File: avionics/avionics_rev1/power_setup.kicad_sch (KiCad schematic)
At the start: 62 parts, among them J1 Conn_01x02, J2 Conn_01x02, J4 USB_C_Receptacle_USB2.0_16P, Q1 DMN2056U-7, U1 LMR604063SBRAKRQ1, U13 TPS2121RUXR, U5 TPS2121RUXR, U6 TLV7041DBVR, U7 TMUX1511RSVR

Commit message: cleaned up schematics after codex work
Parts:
- removed R5: 120 1%, Resistor_SMD:R_0201_0603Metric, symbol Device:R_Small_US
- added C45, C53, C54, C55: 10n 16V, Capacitor_SMD:C_0402_1005Metric, symbol rocketry_library:GRM155R71C103KA01D
- added R5: 120 1%, Resistor_SMD:R_0402_1005Metri, symbol rocketry_library:RC0402FR-071KL
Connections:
- net +3.3V: now also R5.2
- net ADC_MAIN: now also C54.1
- net ADC_USB: now also C53.1
- net GND: now also C45.2, C53.2, C54.2, C55.2; no longer U7.13 (D4), U7.14 (S4), U7.15 (SEL4)
- net SENSE_EN: now also U7.15 (SEL4)
- net at D1.2 (A): now also R5.1
- net ADC_TPS_OUT renamed ADC_PYRO_POWER
- net ADC_PYRO_POWER: now also C55.1
- net SENS_BATT renamed SENS_LOGIC_VIN
- net SENS_LOGIC_VIN: now also U7.14 (S4)
- new net ADC_LOGIC: C45.1, U7.13 (D4)
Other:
- note added: "D1: existing LED reused for MCU status. PB6 high = ON; 1k limits current to ~1.2 mA."
- note added: "U7 CH4: VIN_LOGIC divider -> ADC_LOGIC / PB1. SENSE_EN low at reset; wait >=5 ms after enable before ADC sampling."
- note added: "VIN_LOGIC sense; not raw battery R3/R4: 220k/47k (ratio 0.1760) 16.8 V -> 2.957 V at SENS_LOGIC_VIN"
- note removed: "R = (V_sup - V_forward) / I_forward R = (3.3 - 2.1) / 0.010A = 120 ohm"
- note removed: "VIN_LOGIC sense; not raw battery R3/R4: 220k/47k (ratio 0.1760) 16.8 V -> 2.957 V at SENS_BATT"
- moved on the sheet: C36, R44, U7

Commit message: saving MCU work before using codex
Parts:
- added TP3, TP4, TP5, TP6, TP7, TP8, TP9: TestPoint, symbol Connector:TestPoint
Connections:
- net +3.3V: now also TP3.1
- net PYRO_POWER: now also TP8.1
- net PYRO_POWER_SENS: now also TP9.1
- net VIN_LOGIC: now also TP4.1
- net VIN_MAIN_BATT: now also TP6.1
- net VIN_PYRO_BATT: now also TP5.1
- net at R25.2, R26.1, U5.5 (OV1)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: now also TP7.1

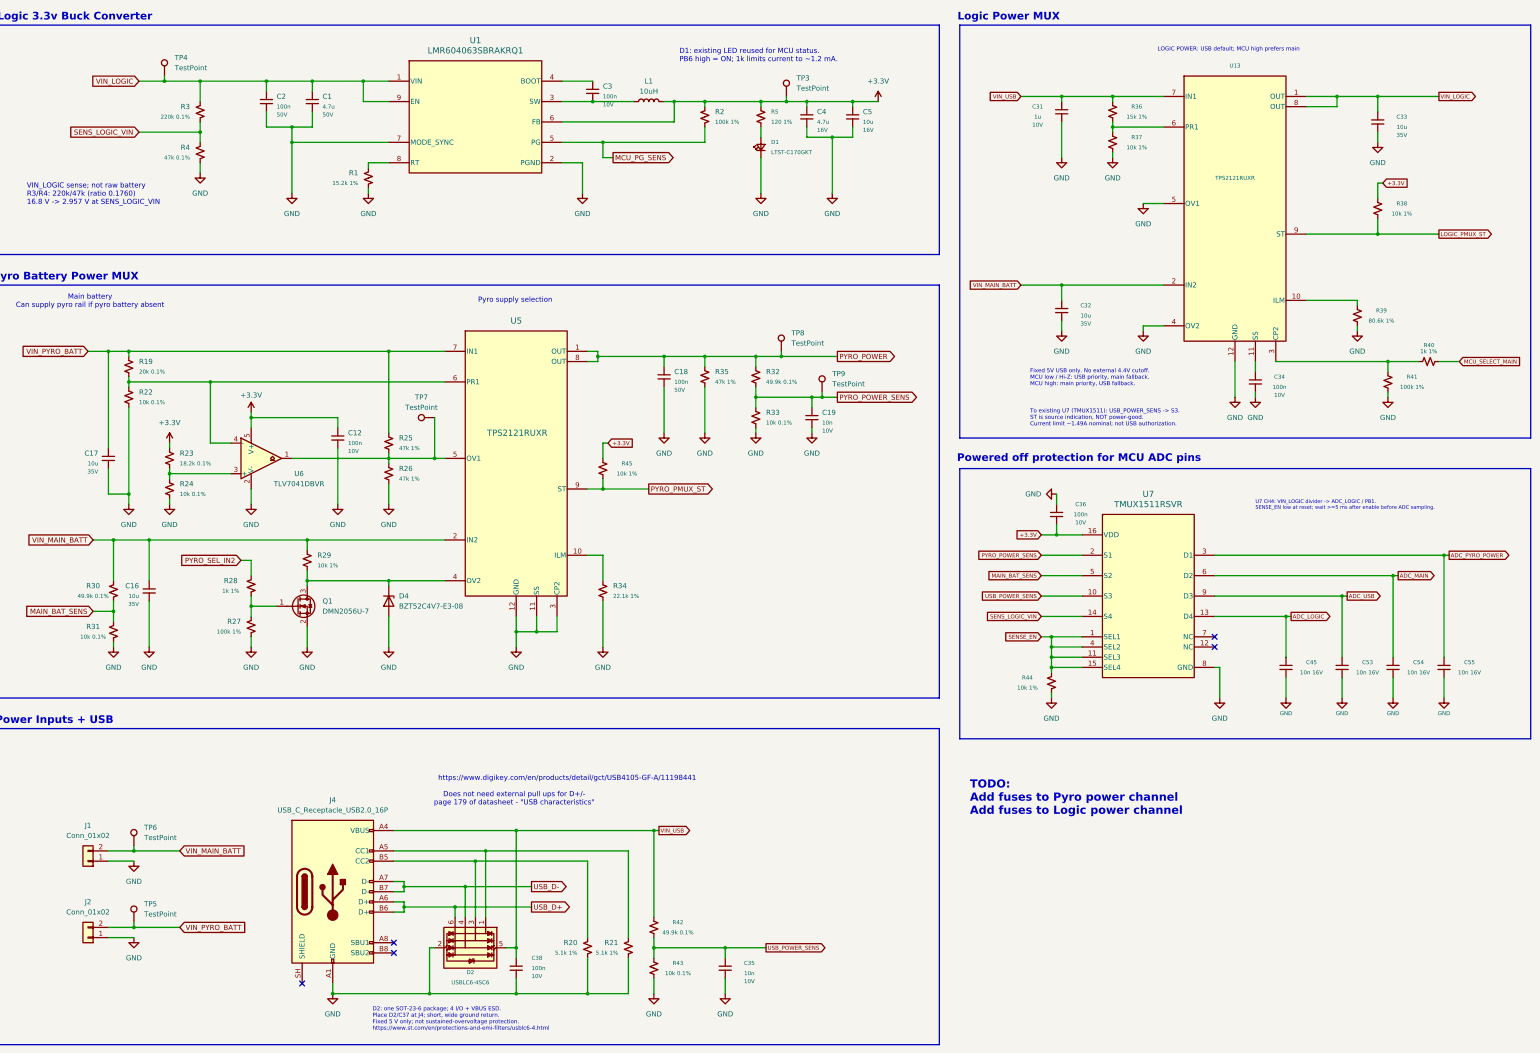
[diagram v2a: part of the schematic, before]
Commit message: fixed ERC errors
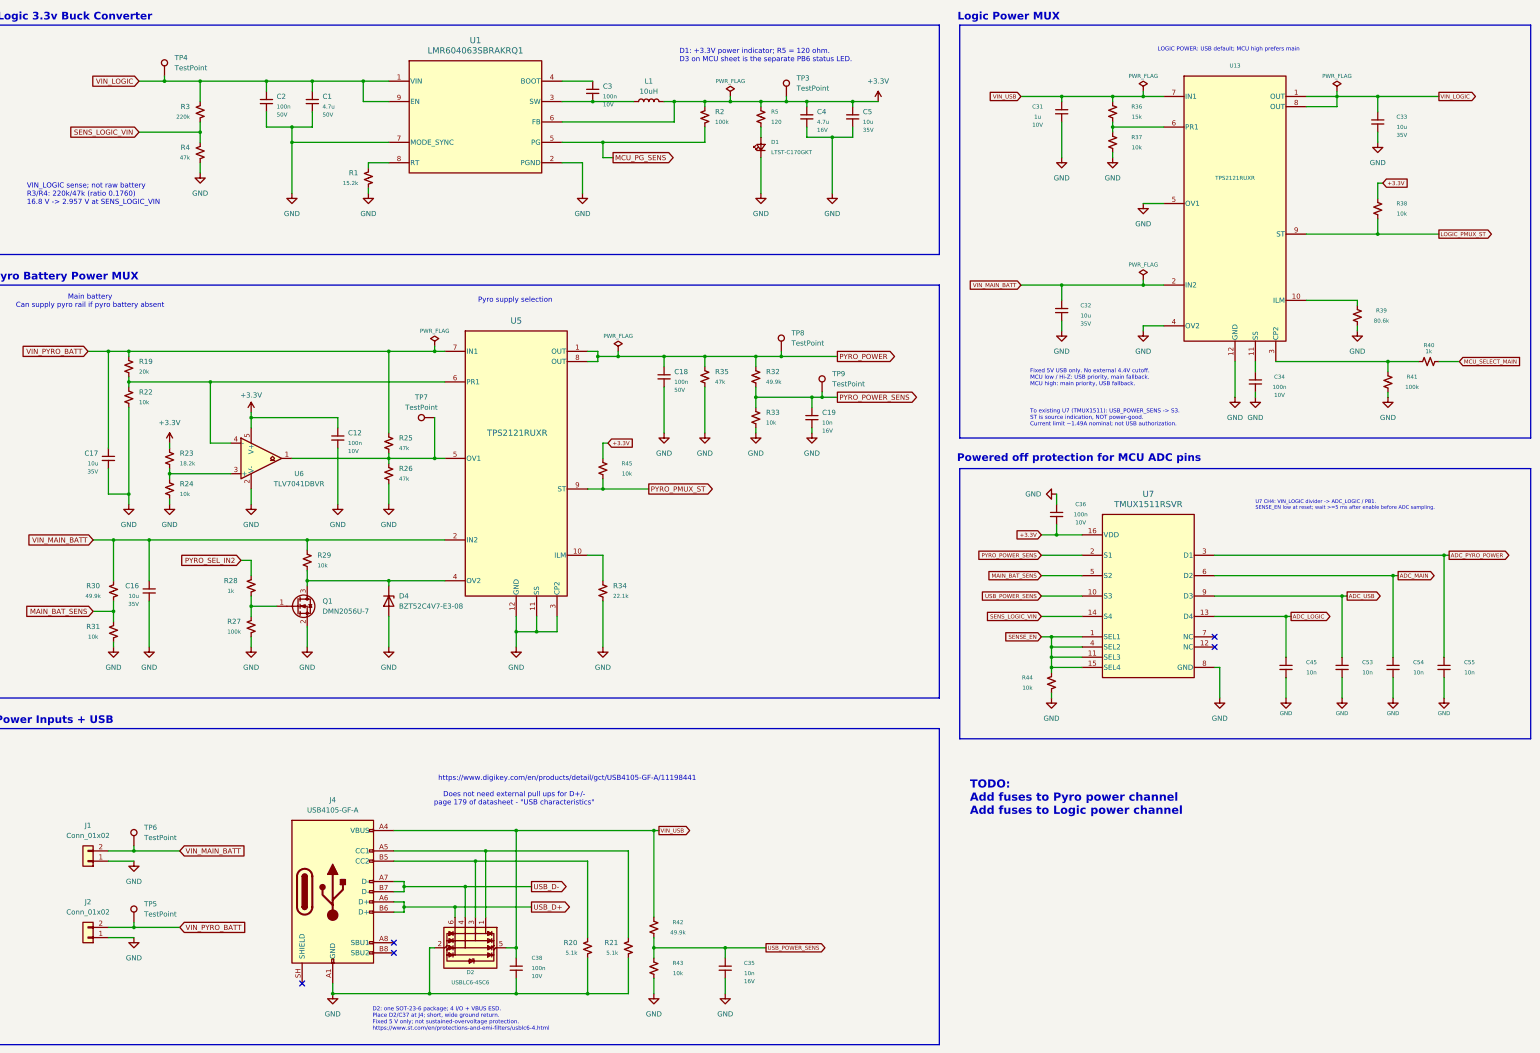
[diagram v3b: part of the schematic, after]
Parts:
- C1: symbol Device:C_Small -> rocketry_library:C2012X5R1H475K125AB; Dielectric X7R -> X5R; DigiKey (none) -> https://www.digikey.com/en/products/detail/tdk/C2012X5R1H47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; MPN (none) -> C2012X5R1H475K125AB; Manufacturer (none) -> TDK; Tolerance (none) -> 10%
- C12, C34, C36, C38: symbol Device:C_Small -> rocketry_library:GRM155R71A104KA01D; DigiKey (none) -> https://www.digikey.com/en/products/detail/murata-electroni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; MPN (none) -> GRM155R71A104KA01D; Tolerance (none) -> 10%
- C16, C17, C32, C33: symbol Device:C_Small -> rocketry_library:GRM21BR6YA106KE43L; Dielectric X7R -> X5R; DigiKey (none) -> https://www.digikey.com/en/products/detail/murata-electroni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; MPN (none) -> GRM21BR6YA106KE43L; Manufacturer (none) -> Murata; Tolerance (none) -> 10%
- C18, C2: symbol Device:C_Small -> rocketry_library:GRM155R71H104KE14D; DigiKey (none) -> https://www.digikey.com/en/products/detail/murata-electroni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; MPN (none) -> GRM155R71H104KE14D; Manufacturer (none) -> Murata; Tolerance (none) -> 10%
- C19, C35: symbol Device:C_Small -> rocketry_library:GRM155R71C103KA01D; DigiKey (none) -> https://www.digikey.com/en/products/detail/murata-electroni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; MPN (none) -> GRM155R71C103KA01D; Tolerance (none) -> 10%; Voltage 10V -> 16V
- C3: footprint Capacitor_SMD:C_0201_0603Metric -> Capacitor_SMD:C_0402_1005Metric; symbol Device:C_Small -> rocketry_library:GRM155R71A104KA01D; DigiKey (none) -> https://www.digikey.com/en/products/detail/murata-electroni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; MPN (none) -> GRM155R71A104KA01D; Tolerance (none) -> 10%
- C31: footprint Capacitor_SMD:C_0402_1005Metric -> Capacitor_SMD:C_0603_1608Metric; symbol Device:C_Small -> rocketry_library:C1608X7R1A105K080AC; DigiKey (none) -> https://www.digikey.com/en/products/detail/tdk/C1608X7R1A10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; MPN (none) -> C1608X7R1A105K080AC; Tolerance (none) -> 10%
- C4: symbol Device:C_Small -> rocketry_library:GRM188R61C475KE11D; Dielectric X7R -> X5R; DigiKey (none) -> https://www.digikey.com/en/products/detail/murata-electroni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; MPN (none) -> GRM188R61C475KE11D; Manufacturer (none) -> Murata; Tolerance (none) -> 10%
- C45, C53, C54, C55: value 10n 16V -> 10n
- C5: symbol Device:C_Small -> rocketry_library:GRM21BR6YA106KE43L; Dielectric X7R -> X5R; DigiKey (none) -> https://www.digikey.com/en/products/detail/murata-electroni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; MPN (none) -> GRM21BR6YA106KE43L; Manufacturer (none) -> Murata; Tolerance (none) -> 10%; Voltage 16V -> 35V
- J4: value USB_C_Receptacle_USB2.0_16P -> USB4105-GF-A; footprint (none) -> Connector_USB:USB_C_Receptacle_GCT_USB4105-xx-A_16P_TopMnt_Horizontal; symbol Connector:USB_C_Receptacle_USB2.0_16P -> rocketry_library:USB4105-GF-A; DigiKey (none) -> https://www.digikey.com/en/products/detail/gct/USB4105-GF-A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; MPN (none) -> USB4105-GF-A; Manufacturer (none) -> GCT
- R1: value 15.2k 1% -> 15.2k; footprint Resistor_SMD:R_0201_0603Metric -> Resistor_SMD:R_0402_1005Metric; symbol Device:R_Small_US -> rocketry_library:RN73R1ETTP1522B25; DigiKey (none) -> https://www.digikey.com/en/products/detail/koa-speer-electr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; MPN (none) -> RN73R1ETTP1522B25; Manufacturer (none) -> KOA Speer; Power (none) -> 0.0625W; Tolerance 1% -> 0.1%; Voltage (none) -> 50V
- R19: value 20k 0.1% -> 20k; footprint (none) -> Resistor_SMD:R_0402_1005Metric; symbol Device:R_Small_US -> rocketry_library:RT0402BRD0720KL; DigiKey (none) -> https://www.digikey.com/en/products/detail/yageo/RT0402BRD0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; MPN (none) -> RT0402BRD0720KL; Manufacturer (none) -> Yageo; Power (none) -> 0.0625W; Voltage (none) -> 50V
- R2, R41: value 100k 1% -> 100k; footprint Resistor_SMD:R_0201_0603Metric -> Resistor_SMD:R_0402_1005Metric; symbol Device:R_Small_US -> rocketry_library:RC0402FR-07100KL; DigiKey (none) -> https://www.digikey.com/en/products/detail/yageo/RC0402FR-0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; MPN (none) -> RC0402FR-07100KL; Power (none) -> 0.063W; Voltage (none) -> 50V
- R20, R21: value 5.1k 1% -> 5.1k; footprint Resistor_SMD:R_0201_0603Metric -> Resistor_SMD:R_0402_1005Metric; symbol Device:R_Small_US -> rocketry_library:RC0402FR-075K1L; DigiKey (none) -> https://www.digikey.com/en/products/detail/yageo/RC0402FR-0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; MPN (none) -> RC0402FR-075K1L; Manufacturer (none) -> Yageo; Power (none) -> 0.0625W; Voltage (none) -> 50V
- R22, R24, R31, R33: value 10k 0.1% -> 10k; footprint (none) -> Resistor_SMD:R_0402_1005Metric; symbol Device:R_Small_US -> rocketry_library:RT0402BRD0710KL; DigiKey (none) -> https://www.digikey.com/en/products/detail/yageo/RT0402BRD0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; MPN (none) -> RT0402BRD0710KL; Manufacturer (none) -> Yageo; Power (none) -> 0.0625W; Voltage (none) -> 50V
- R23: value 18.2k 0.1% -> 18.2k; footprint (none) -> Resistor_SMD:R_0402_1005Metric; symbol Device:R_Small_US -> rocketry_library:RT0402BRD0718K2L; DigiKey (none) -> https://www.digikey.com/en/products/detail/yageo/RT0402BRD0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; MPN (none) -> RT0402BRD0718K2L; Manufacturer (none) -> Yageo; Power (none) -> 0.0625W; Voltage (none) -> 50V
- R25, R26, R35: value 47k 1% -> 47k; footprint (none) -> Resistor_SMD:R_0402_1005Metric; symbol Device:R_Small_US -> rocketry_library:RC0402FR-0747KL; DigiKey (none) -> https://www.digikey.com/en/products/detail/yageo/RC0402FR-0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; MPN (none) -> RC0402FR-0747KL; Manufacturer (none) -> Yageo; Power (none) -> 0.0625W; Voltage (none) -> 50V
- R27: value 100k 1% -> 100k; footprint (none) -> Resistor_SMD:R_0402_1005Metric; symbol Device:R_Small_US -> rocketry_library:RC0402FR-07100KL; DigiKey (none) -> https://www.digikey.com/en/products/detail/yageo/RC0402FR-0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; MPN (none) -> RC0402FR-07100KL; Power (none) -> 0.063W; Voltage (none) -> 50V
- R28: value 1k 1% -> 1k; footprint (none) -> Resistor_SMD:R_0402_1005Metric; symbol Device:R_Small_US -> rocketry_library:RC0402FR-071KL; DigiKey (none) -> https://www.digikey.com/en/products/detail/yageo/RC0402FR-0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; MPN (none) -> RC0402FR-071KL; Power (none) -> 0.063W; Voltage (none) -> 50V
- R29: value 10k 1% -> 10k; footprint (none) -> Resistor_SMD:R_0402_1005Metric; symbol Device:R_Small_US -> rocketry_library:RC0402FR-0710KL; DigiKey (none) -> https://www.digikey.com/en/products/detail/yageo/RC0402FR-0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; MPN (none) -> RC0402FR-0710KL; Voltage (none) -> 50V
- R3: value 220k 0.1% -> 220k; footprint Resistor_SMD:R_0201_0603Metric -> Resistor_SMD:R_0402_1005Metric; symbol Device:R_Small_US -> rocketry_library:RT0402BRD07220KL; DigiKey (none) -> https://www.digikey.com/en/products/detail/yageo/RT0402BRD0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; MPN (none) -> RT0402BRD07220KL; Manufacturer (none) -> Yageo; Power (none) -> 0.0625W; Voltage (none) -> 50V
- R30, R32: value 49.9k 0.1% -> 49.9k; footprint (none) -> Resistor_SMD:R_0402_1005Metric; symbol Device:R_Small_US -> rocketry_library:RT0402BRD0749K9L; DigiKey (none) -> https://www.digikey.com/en/products/detail/yageo/RT0402BRD0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; MPN (none) -> RT0402BRD0749K9L; Manufacturer (none) -> Yageo; Power (none) -> 0.0625W; Voltage (none) -> 50V
- R34: value 22.1k 1% -> 22.1k; footprint (none) -> Resistor_SMD:R_0402_1005Metric; symbol Device:R_Small_US -> rocketry_library:RC0402FR-0722K1L; DigiKey (none) -> https://www.digikey.com/en/products/detail/yageo/RC0402FR-0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; MPN (none) -> RC0402FR-0722K1L; Manufacturer (none) -> Yageo; Power (none) -> 0.0625W; Voltage (none) -> 50V
- R36: value 15k 1% -> 15k; footprint Resistor_SMD:R_0201_0603Metric -> Resistor_SMD:R_0402_1005Metric; symbol Device:R_Small_US -> rocketry_library:RC0402FR-0715KL; DigiKey (none) -> https://www.digikey.com/en/products/detail/yageo/RC0402FR-0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; MPN (none) -> RC0402FR-0715KL; Manufacturer (none) -> Yageo; Power (none) -> 0.0625W; Voltage (none) -> 50V
- R37, R38, R44, R45: value 10k 1% -> 10k; footprint Resistor_SMD:R_0201_0603Metric -> Resistor_SMD:R_0402_1005Metric; symbol Device:R_Small_US -> rocketry_library:RC0402FR-0710KL; DigiKey (none) -> https://www.digikey.com/en/products/detail/yageo/RC0402FR-0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; MPN (none) -> RC0402FR-0710KL; Voltage (none) -> 50V
- R39: value 80.6k 1% -> 80.6k; footprint Resistor_SMD:R_0201_0603Metric -> Resistor_SMD:R_0402_1005Metric; symbol Device:R_Small_US -> rocketry_library:RC0402FR-0780K6L; DigiKey (none) -> https://www.digikey.com/en/products/detail/yageo/RC0402FR-0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; MPN (none) -> RC0402FR-0780K6L; Manufacturer (none) -> Yageo; Power (none) -> 0.0625W; Voltage (none) -> 50V
- R4: value 47k 0.1% -> 47k; footprint Resistor_SMD:R_0201_0603Metric -> Resistor_SMD:R_0402_1005Metric; symbol Device:R_Small_US -> rocketry_library:RT0402BRD0747KL; DigiKey (none) -> https://www.digikey.com/en/products/detail/yageo/RT0402BRD0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; MPN (none) -> RT0402BRD0747KL; Manufacturer (none) -> Yageo; Power (none) -> 0.0625W; Voltage (none) -> 50V
- R40: value 1k 1% -> 1k; footprint Resistor_SMD:R_0201_0603Metric -> Resistor_SMD:R_0402_1005Metric; symbol Device:R_Small_US -> rocketry_library:RC0402FR-071KL; DigiKey (none) -> https://www.digikey.com/en/products/detail/yageo/RC0402FR-0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; MPN (none) -> RC0402FR-071KL; Power (none) -> 0.063W; Voltage (none) -> 50V
- R42: value 49.9k 0.1% -> 49.9k; footprint Resistor_SMD:R_0201_0603Metric -> Resistor_SMD:R_0402_1005Metric; symbol Device:R_Small_US -> rocketry_library:RT0402BRD0749K9L; DigiKey (none) -> https://www.digikey.com/en/products/detail/yageo/RT0402BRD0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; MPN (none) -> RT0402BRD0749K9L; Manufacturer (none) -> Yageo; Power (none) -> 0.0625W; Voltage (none) -> 50V
- R43: value 10k 0.1% -> 10k; footprint Resistor_SMD:R_0201_0603Metric -> Resistor_SMD:R_0402_1005Metric; symbol Device:R_Small_US -> rocketry_library:RT0402BRD0710KL; DigiKey (none) -> https://www.digikey.com/en/products/detail/yageo/RT0402BRD0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; MPN (none) -> RT0402BRD0710KL; Manufacturer (none) -> Yageo; Power (none) -> 0.0625W; Voltage (none) -> 50V
- R5: value 120 1% -> 120; footprint Resistor_SMD:R_0402_1005Metri -> Resistor_SMD:R_0402_1005Metric; symbol rocketry_library:RC0402FR-071KL -> rocketry_library:RC0402FR-07120RL; DigiKey https://www.digikey.com/en/products/detail/yageo/RC0402FR-071KL/726513 -> https://www.digikey.com/en/products/detail/yageo/RC0402FR-07120RL/726535; MPN RC0402FR-071KL -> RC0402FR-07120RL; Manufacturer (none) -> Yageo; Power 0.063W -> 0.0625W
- TP3, TP4, TP5, TP6, TP7, TP8, TP9: footprint (none) -> TestPoint:TestPoint_Pad_D1.0mm; now left out of the parts list
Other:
- note added: "D1: +3.3V power indicator; R5 = 120 ohm. D3 on MCU sheet is the separate PB6 status LED."
- note removed: "D1: existing LED reused for MCU status. PB6 high = ON; 1k limits current to ~1.2 mA."
